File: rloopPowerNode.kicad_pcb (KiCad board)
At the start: 4 copper layers, 150 x 200 mm, 132 parts, among them P1 CONN_01X02, P10 CONN_01X02, P11 CONN_01X03, P12 CONN_01X03, P13 CONN_01X02, P14 CONN_01X02, P15 CONN_01X02, P16 CONN_01X02, P17 AMPMODU-02X05, P18 SHUNT, P19 CONN_01X02, P2 CONN_01X02, P20 CONN_01X02, P21 CONN_01X02, P22 CONN_01X02, P23 CONN_01X02, P24 CONN_01X02, P25 CONN_02X02, P26 CONN_02X02, P27 CONN_01X02, P28 CONN_01X02, P29 CONN_01X02, P3 CONN_01X02, P30 CONN_01X02, P31 CONN_02X02, P32 CONN_01X02, P33 CONN_02X02, P34 CONN_01X02, P4 CONN_01X02, P5 CONN_01X01, P5 CONN_01X04, P6 CONN_01X02, P7 CONN_01X03, P8 CONN_01X03, P9 CONN_01X02, Q1 PMOS, Q2 NMOS, Q3 BSS84, Q4 NMOS, Q5 NMOS, Q6 NMOS, Q7 NMOS, U1 CPC1718, U10 AMC1100, U2 CPC1718, U3 H11F1SM, U4 MAX6814, U5 CPC1718, U6 CPC1718, U7 DS2482-100, U8 MS5607-02BA03, U9 78L05

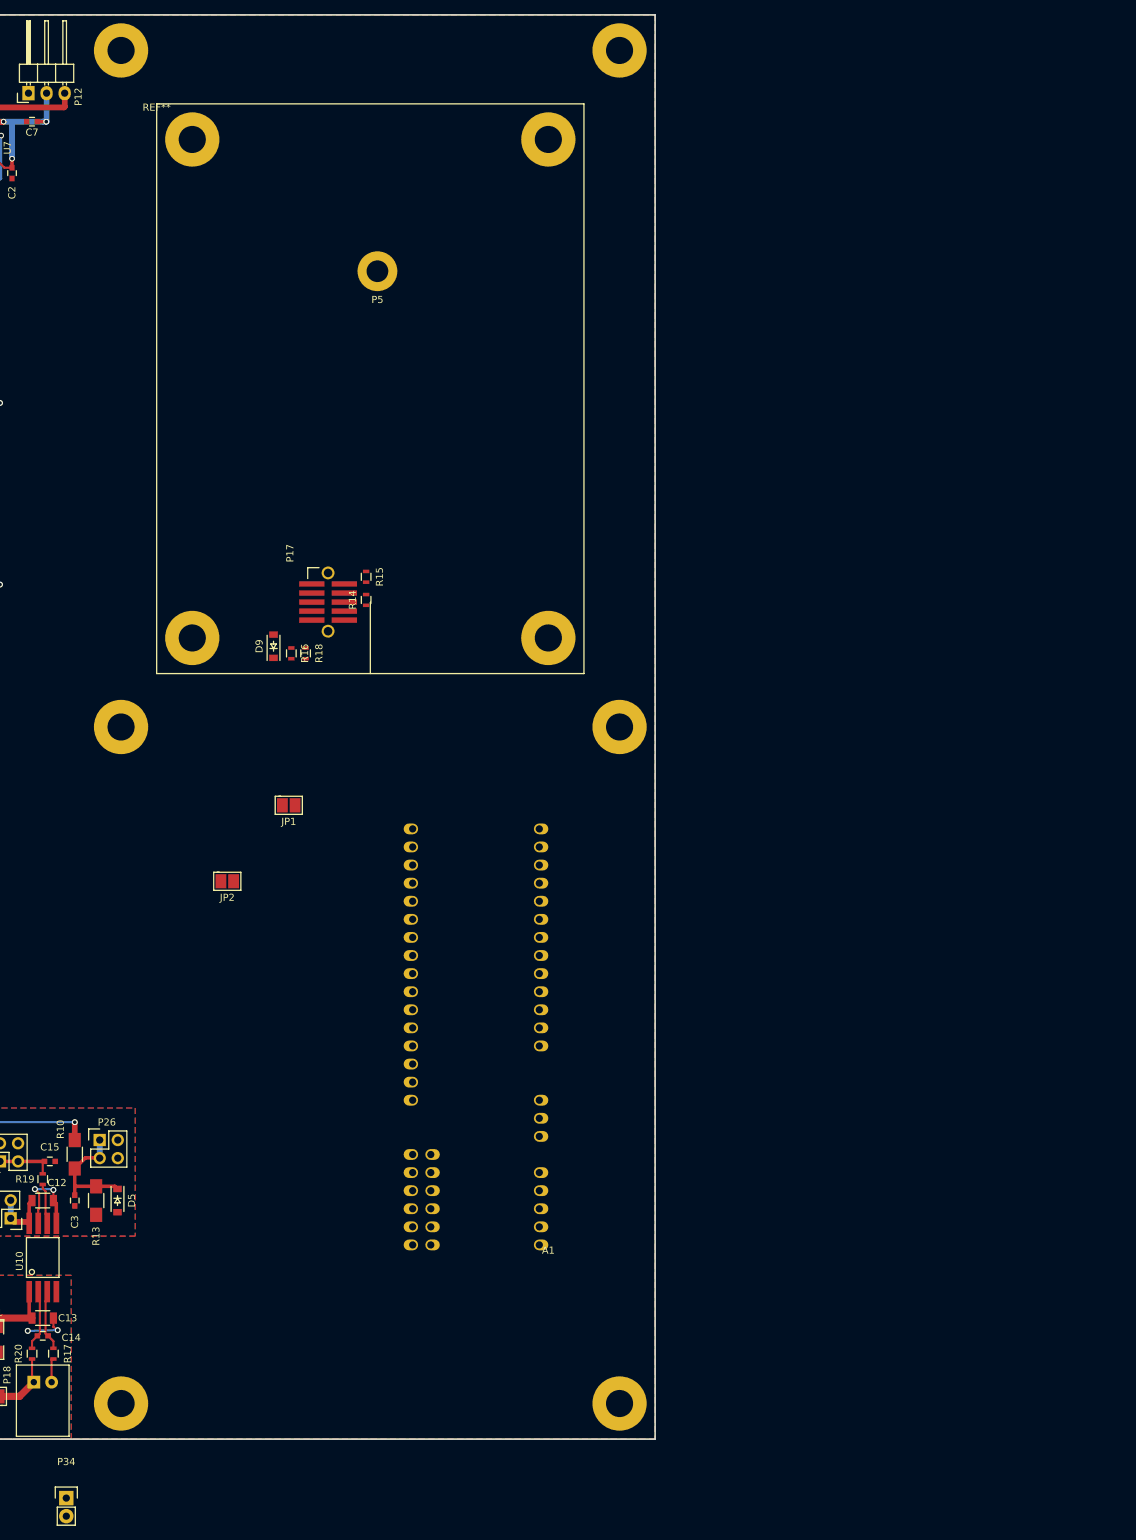
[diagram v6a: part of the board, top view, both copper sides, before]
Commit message: laid out BMS section
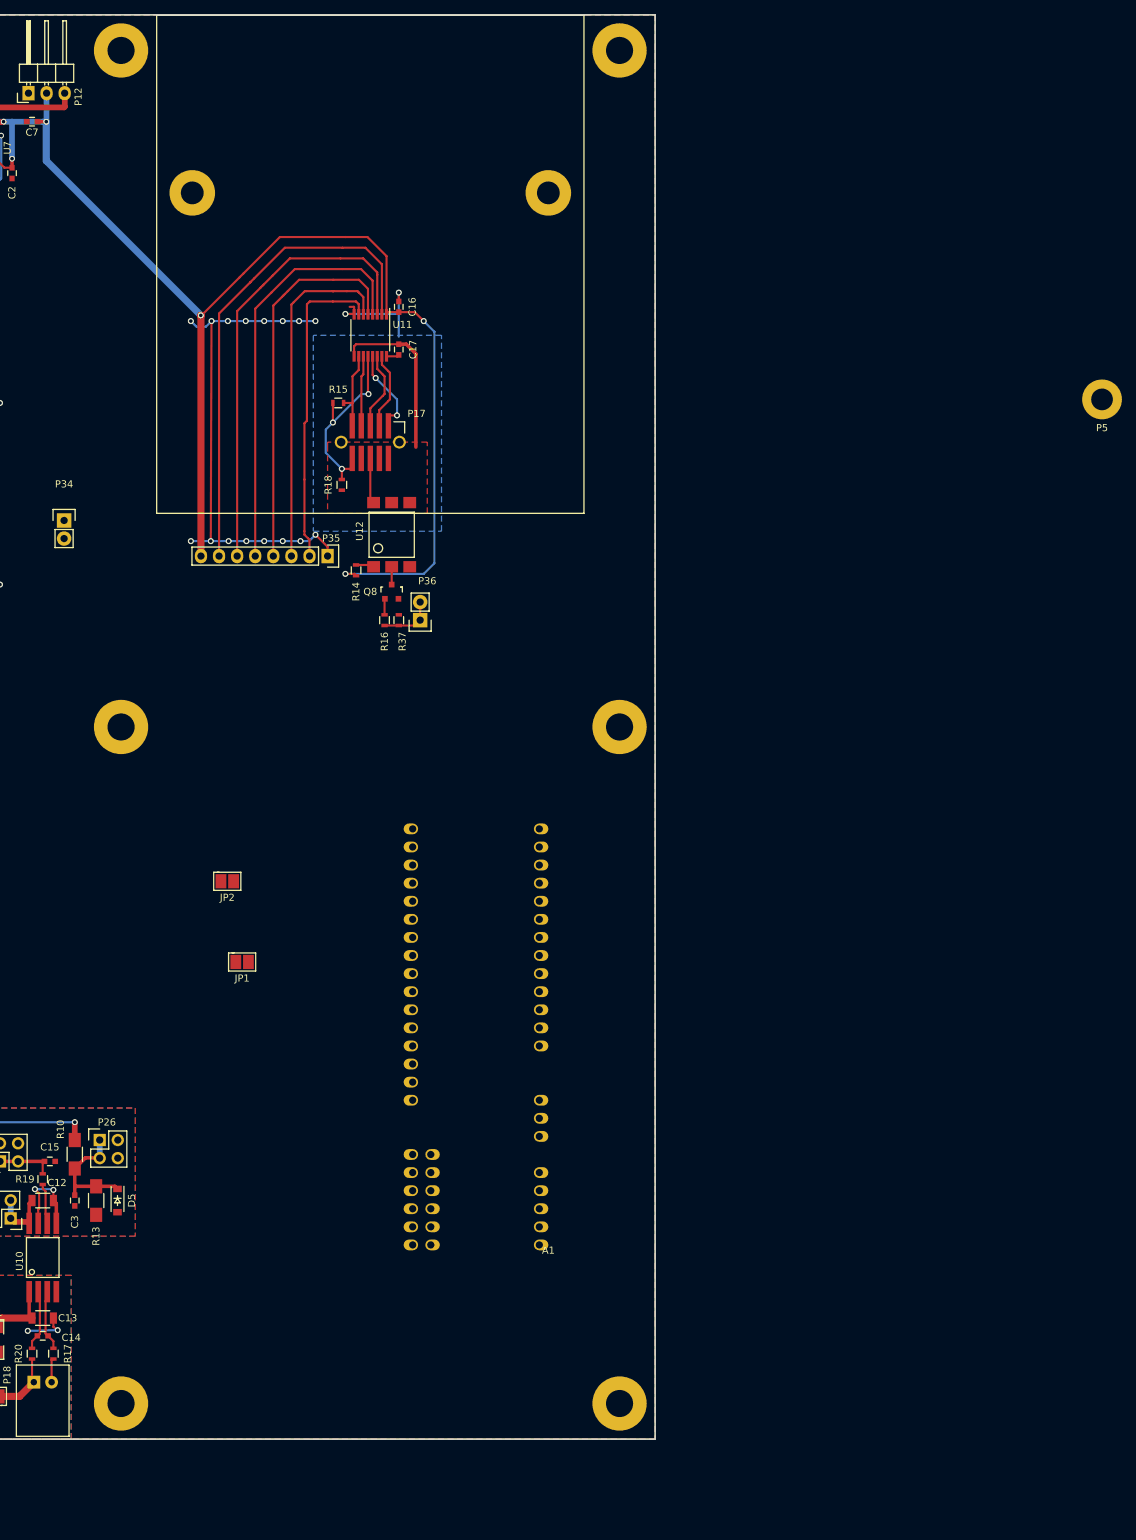
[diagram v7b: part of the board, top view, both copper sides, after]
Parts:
- removed D9: ZENER +3V6, Diodes_SMD:SOD-123
- removed REF**: BMS-PCB-OUTLINE, -footprints:BMS-PCB-OUTLINE
- added C16: 100n, Capacitors_SMD:C_0603, F.Cu at (149.0, 76.0)
- added C17: 100n, Capacitors_SMD:C_0603, F.Cu at (149.0, 82.0)
- added P35: CONN_01X08, Pin_Headers:Pin_Header_Straight_1x08, F.Cu at (139.0, 111.0)
- added P36: CONN_01X02, Pin_Headers:Pin_Header_Straight_1x02, F.Cu at (152.0, 120.0)
- added Q8: Q_NMOS, TO_SOT_Packages_SMD:SOT-23, F.Cu at (148.0, 116.0)
- added R37: 100K, Resistors_SMD:R_0603, F.Cu at (149.0, 120.0)
- added U11: MAX14850, Housings_SSOP:TSSOP-16_4.4x5mm_Pitch0.65mm, F.Cu at (145.0, 80.0)
- added U12: H11F1SM, -footprints:OPTOCOUPLER-0.1in-6pin-SMD, F.Cu at (148.0, 108.0)
- P17: footprint -footprints:AMPMODU-MALE-02X05-0.05in -> -footprints:BMS
- R14: value 10K -> 470
- R15: value 10K -> 100K
- moved P34 137.3 mm to (102.0, 106.0)
- moved P5 103.3 mm to (247.8, 89.0)
- moved R15 24.7 mm to (140.5, 89.5), turned to 0 degrees
- moved R18 24.2 mm to (141.0, 101.0), turned to 90 degrees
- moved P17 23.2 mm to (145.0, 95.0), turned to 270 degrees
- moved JP1 23.0 mm to (127.0, 168.0)
- moved R16 13.9 mm to (147.0, 120.0), turned to 90 degrees
- moved R14 4.39 mm to (143.0, 113.0), turned to 270 degrees
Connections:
- A1 pad A10: BMS-PWRAVAIL -> Net-(A1-PadA10)
- A1 pad A11: BMS-PWREN -> Net-(A1-PadA11)
- A1 pad A12: BMS-PWRDN -> Net-(A1-PadA12)
- A1 pad T32: GNDFAULT-PWM -> BMS-PWRAVAIL
- A1 pad T33: /GNDFAULT -> BMS-IRQ
- P17 pad 1: BMS-MISO -> BMS-MISO-HI
- P17 pad 10: GND -> BMS-PWRAVAIL-HI
- P17 pad 2: BMS-PWREN -> GND-BMS
- P17 pad 3: BMS-MOSI -> BMS-MOSI-HI
- P17 pad 4: BMS-PWRDN -> Net-(P17-Pad4)
- P17 pad 5: BMS-SCK -> BMS-SCK-HI
- P17 pad 6: GND -> Net-(P17-Pad6)
- P17 pad 7: BMS-CS -> BMS-CS-HI
- P17 pad 8: GND -> Net-(P17-Pad8)
- P17 pad 9: Net-(P17-Pad9) -> BMS-IRQ-HI
- P17 pad M1: GND -> Net-(P17-PadM1)
- P17 pad M2: GND -> Net-(P17-PadM2)
- R14 pad 1: GND -> Net-(R14-Pad1)
- R14 pad 2: BMS-PWRDN -> +3V3
- R15 pad 1: GND -> BMS-PWRAVAIL-HI
- R15 pad 2: BMS-PWREN -> BMS-IRQ-HI
- R16 pad 1: Net-(P17-Pad9) -> BMS-PD
- R16 pad 2: BMS-PWRAVAIL -> Net-(Q8-Pad1)
- R18 pad 1: GND -> GND-BMS
- R18 pad 2: BMS-PWRAVAIL -> BMS-PWRAVAIL-HI
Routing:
- net +3V3: track 97.4 -> 262.8 mm, vias 7 -> 10
- net GND: track 363.4 -> 452.1 mm, vias 45 -> 63
- net BMS-MOSI: track 0.00 -> 68.7 mm
- net BMS-SCK: track 0.00 -> 63.9 mm
- net BMS-MISO: track 0.00 -> 58.9 mm
- net BMS-PWRAVAIL: track 0.00 -> 54.1 mm
- net BMS-CS: track 0.00 -> 49.2 mm
- net BMS-IRQ: track 0.00 -> 44.8 mm
- net BMS-PWRAVAIL-HI: track 0.00 -> 27.1 mm, vias 0 -> 3
- net GND-BMS: track 0.00 -> 23.9 mm
- net BMS-MISO-HI: track 0.00 -> 12.8 mm, vias 0 -> 2
- net BMS-IRQ-HI: track 0.00 -> 11.4 mm
- net BMS-SCK-HI: track 0.00 -> 11.0 mm
- net BMS-MOSI-HI: track 0.00 -> 10.9 mm
- net BMS-CS-HI: track 0.00 -> 9.88 mm
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- added copper zone on F.Cu, net GND-BMS
